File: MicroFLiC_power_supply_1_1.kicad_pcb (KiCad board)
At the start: 2 copper layers, 49.8 x 49.8 mm, 64 parts, among them P1 BARREL_JACK, P2 CONN_02X03, P3 Socket_1x14, P4 Socket_2x2, P6 JUMPER3, Q1 SI2369, Q2 TSM2314, Q3 SI2369, Q4 IRF8721, SW1 SW_PUSH_RA, U1 AP1117E33, U2 ADP2381, U3 TPS54428

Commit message: Added load resistor. Changed part references in consequence.
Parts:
- added R10: 10k, Resistors_SMD:R_0805, F.Cu at (123.2, 118.0)
- BT1: value ML2016 -> 3V LiMnO2
- C12, C13: value 10u -> 10u/10V/0.15Ω<ESR<0.5Ω
- D1, D2: value PMEG2020 -> 1N4148
- moved D1 1.27 mm to (132.6, 109.5)
- renumbered R10 to R11, R11 to R12, R12 to R13, R13 to R14, R14 to R15, R15 to R16, R16 to R17, R17 to R18
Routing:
- net /electronicSwitch/MCU_OFF: track 63.2 -> 61.9 mm
- net /electronicSwitch/PUSHBUTTON: track 25.3 -> 24.7 mm

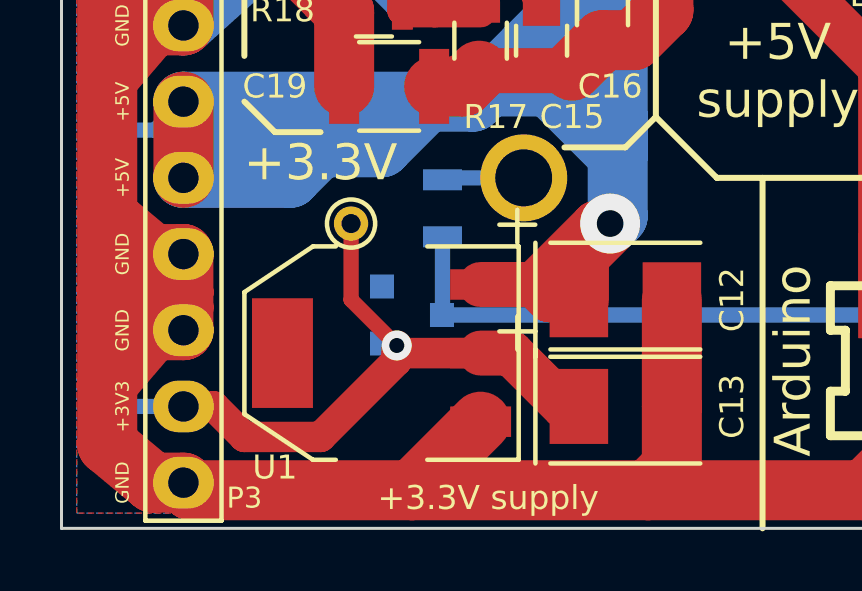
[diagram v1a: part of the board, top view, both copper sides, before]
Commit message: Changed BAR43S diode into 1N4148 for minimum leakage current.
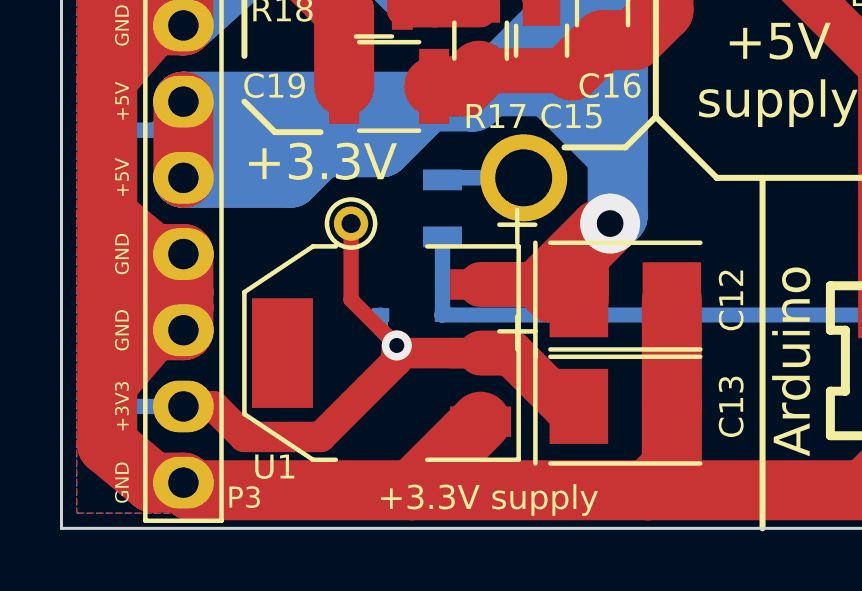
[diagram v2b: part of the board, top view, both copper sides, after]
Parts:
- D3: value BAR43S -> 1N4148; footprint Housings_SOT-23_SOT-143_TSOT-6:SOT-23 -> Diodes_SMD:SOD-323
- turned D3 to 180 degrees
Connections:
- D3 pad 1: +3V3 -> +BATT
- D3 pad 2: (no net) -> +3V3
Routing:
- net +3V3: track 23.6 -> 24.4 mm
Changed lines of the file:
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@@
   (general
     (links 140)
-    (no_connects 0)
+    (no_connects 2)
     (area 100.025999 100.025999 149.910001 149.910001)
     (thickness 1.6)
     (drawings 70)
-    (tracks 671)
+    (tracks 672)
     (zones 0)
     (modules 65)
@@
   (page A4)
   (layers
-    (0 F.Cu signal)
-    (31 B.Cu signal hide)
+    (0 F.Cu signal hide)
+    (31 B.Cu signal)
     (32 B.Adhes user)
     (33 F.Adhes user)
@@
   )
   (setup
-    (last_trace_width 0.254)
+    (last_trace_width 0.508)
     (user_trace_width 0.254)
     (user_trace_width 0.381)
@@
     )
   )
-  (module Housings_SOT-23_SOT-143_TSOT-6:SOT-23 (layer B.Cu)
-    (at 111.76 142.748 90)
-    (descr "SOT-23, Standard")
-    (tags SOT-23)
-    (attr smd)
-    (fp_text reference D3 (at 0 2.25 90) (layer B.SilkS)
-      (effects (font (size 1 1) (thickness 0.15)) (justify mirror))
-    )
-    (fp_text value BAR43S (at 0 -2.3 90) (layer B.Fab) hide
-      (effects (font (size 1 1) (thickness 0.15)) (justify mirror))
-    )
-    (fp_line (start -1.65 1.6) (end 1.65 1.6) (layer B.CrtYd) (width 0.05))
-    (fp_line (start 1.65 1.6) (end 1.65 -1.6) (layer B.CrtYd) (width 0.05))
-    (fp_line (start 1.65 -1.6) (end -1.65 -1.6) (layer B.CrtYd) (width 0.05))
-    (fp_line (start -1.65 -1.6) (end -1.65 1.6) (layer B.CrtYd) (width 0.05))
-    (fp_line (start 1.29916 0.65024) (end 1.2509 0.65024) (layer B.SilkS) (width 0.15))
-    (fp_line (start -1.49982 -0.0508) (end -1.49982 0.65024) (layer B.SilkS) (width 0.15))
-    (fp_line (start -1.49982 0.65024) (end -1.2509 0.65024) (layer B.SilkS) (width 0.15))
-    (fp_line (start 1.29916 0.65024) (end 1.49982 0.65024) (layer B.SilkS) (width 0.15))
-    (fp_line (start 1.49982 0.65024) (end 1.49982 -0.0508) (layer B.SilkS) (width 0.15))
-    (pad 1 smd rect (at -0.95 -1.00076 90) (size 0.8001 0.8001) (layers B.Cu B.Paste B.Mask)
-      (net 10 +3V3))
-    (pad 2 smd rect (at 0.95 -1.00076 90) (size 0.8001 0.8001) (layers B.Cu B.Paste B.Mask))
-    (pad 3 smd rect (at 0 0.99822 90) (size 0.8001 0.8001) (layers B.Cu B.Paste B.Mask)
-      (net 15 +BATT))
-    (model SMD_Packages.3dshapes/SOT-23_Inv.wrl
-      (at (xyz 0 0 0))
-      (scale (xyz 0.3937 0.3937 0.3937))
-      (rotate (xyz 0 0 180))
-    )
-  )
   (module jakub:ML2016 (layer B.Cu)
     (at 125.984 138.176 180)
@@
       (rotate (xyz 0 0 0))
     )
+  )
+  (module Diodes_SMD:SOD-323 (layer B.Cu)
+    (at 111.76 142.748 180)
+    (descr SOD-323)
+    (tags SOD-323)
+    (attr smd)
+    (fp_text reference D3 (at 2.286 0 180) (layer B.SilkS)
+      (effects (font (size 0.8 0.8) (thickness 0.12)) (justify mirror))
+    )
+    (fp_text value 1N4148 (at 0.1 -1.9 180) (layer B.Fab)
+      (effects (font (size 1 1) (thickness 0.15)) (justify mirror))
+    )
+    (fp_line (start 0.25 0) (end 0.5 0) (layer B.SilkS) (width 0.15))
+    (fp_line (start -0.25 0) (end -0.5 0) (layer B.SilkS) (width 0.15))
+    (fp_line (start -0.25 0) (end 0.25 0.35) (layer B.SilkS) (width 0.15))
+    (fp_line (start 0.25 0.35) (end 0.25 -0.35) (layer B.SilkS) (width 0.15))
+    (fp_line (start 0.25 -0.35) (end -0.25 0) (layer B.SilkS) (width 0.15))
+    (fp_line (start -0.25 0.35) (end -0.25 -0.35) (layer B.SilkS) (width 0.15))
+    (fp_line (start -1.5 0.95) (end 1.5 0.95) (layer B.CrtYd) (width 0.05))
+    (fp_line (start 1.5 0.95) (end 1.5 -0.95) (layer B.CrtYd) (width 0.05))
+    (fp_line (start -1.5 -0.95) (end 1.5 -0.95) (layer B.CrtYd) (width 0.05))
+    (fp_line (start -1.5 0.95) (end -1.5 -0.95) (layer B.CrtYd) (width 0.05))
+    (fp_line (start -1.3 -0.8) (end 1.1 -0.8) (layer B.SilkS) (width 0.15))
+    (fp_line (start -1.3 0.8) (end 1.1 0.8) (layer B.SilkS) (width 0.15))
+    (pad 1 smd rect (at -1.055 0 180) (size 0.59 0.45) (layers B.Cu B.Paste B.Mask)
+      (net 15 +BATT))
+    (pad 2 smd rect (at 1.055 0 180) (size 0.59 0.45) (layers B.Cu B.Paste B.Mask)
+      (net 10 +3V3))
   )
   (gr_line (start 131.572 119.888) (end 121.92 119.888) (layer F.SilkS) (width 0.2))
@@
   (segment (start 125.476 125.984) (end 127.508 128.016) (width 2) (layer F.Cu) (net 9))
   (segment (start 124.282 125.984) (end 125.476 125.984) (width 2) (layer F.Cu) (net 9))
+  (segment (start 110.705 142.748) (end 110.705 143.217) (width 0.508) (layer B.Cu) (net 10))
+  (segment (start 110.705 143.217) (end 111.252 143.764) (width 0.508) (layer B.Cu) (net 10))
   (segment (start 109.728 139.7) (end 109.728 142.24) (width 0.508) (layer F.Cu) (net 10))
   (segment (start 109.728 142.24) (end 111.252 143.764) (width 0.508) (layer F.Cu) (net 10))
@@
   (via (at 111.252 143.764) (size 1) (layers F.Cu B.Cu) (net 10))
   (segment (start 111.252 143.764) (end 111.252 144.018) (width 0.508) (layer F.Cu) (net 10))
-  (segment (start 110.75924 143.698) (end 111.186 143.698) (width 0.508) (layer B.Cu) (net 10))
   (segment (start 102.042 145.796) (end 101.6 146.238) (width 0.508) (layer B.Cu) (net 10))
   (segment (start 104.14 145.796) (end 102.042 145.796) (width 0.508) (layer B.Cu) (net 10))

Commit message: Added detailed part descriptions
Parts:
- BT1: value 3V LiMnO2 -> 3V LiMnO₂
- C1, C15, C8: value 1u -> 1u/50V
- C10, C11, C19: value 47u/6.3V -> 47u/16V
- C4: value 10u/25V -> 4u7/25V
- P1: value BARREL_JACK -> DC jack
- P2: value CONN_02X03 -> 6-way Micro-MaTch
- P3: value Socket_1x14 -> 1x14 socket strip
- P4: value Socket_2x2 -> 2x2 socket strip
- P6: value JUMPER3 -> 1x3 header strip
- SW1: value SW_PUSH_RA -> Tactile switch R/A
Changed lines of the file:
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@@
-(kicad_pcb (version 4) (host pcbnew 4.0.1-3.201512221402+6198~38~ubuntu14.04.1-stable)
+(kicad_pcb (version 4) (host pcbnew 4.0.2-4+6225~38~ubuntu14.04.1-stable)
   (general
     (links 140)
-    (no_connects 2)
+    (no_connects 0)
     (area 100.025999 100.025999 149.910001 149.910001)
     (thickness 1.6)
@@
       (effects (font (size 1 1) (thickness 0.15)) (justify mirror))
     )
-    (fp_text value "3V LiMnO2" (at 10.16 -9.652 180) (layer B.SilkS)
+    (fp_text value "3V LiMnO₂" (at 10.16 -9.652 180) (layer B.SilkS)
       (effects (font (size 1 1) (thickness 0.15)) (justify mirror))
     )
@@
       (effects (font (size 0.8 0.8) (thickness 0.12)))
     )
-    (fp_text value BARREL_JACK (at -5.08 5.588 270) (layer F.Fab) hide
+    (fp_text value "DC jack" (at -5.08 5.588 270) (layer F.Fab) hide
       (effects (font (size 1 1) (thickness 0.15)))
     )
@@
       (effects (font (size 0.8 0.8) (thickness 0.12)))
     )
-    (fp_text value CONN_02X03 (at -5.715 0 90) (layer F.SilkS) hide
+    (fp_text value "6-way Micro-MaTch" (at -5.715 0 90) (layer F.SilkS) hide
       (effects (font (size 1 1) (thickness 0.15)))
     )
@@
       (effects (font (size 0.8 0.8) (thickness 0.12)))
     )
-    (fp_text value JUMPER3 (at 0 -3.1 270) (layer F.Fab) hide
+    (fp_text value "1x3 header strip" (at 0 -3.1 270) (layer F.Fab) hide
       (effects (font (size 1 1) (thickness 0.15)))
     )
@@
       (effects (font (size 1 1) (thickness 0.15)))
     )
-    (fp_text value SW_PUSH_RA (at 0 3.175) (layer F.Fab) hide
+    (fp_text value "Tactile switch R/A" (at 0 3.175) (layer F.Fab) hide
       (effects (font (size 1 1) (thickness 0.15)))
     )
@@
       (effects (font (size 0.8 0.8) (thickness 0.12)))
     )
-    (fp_text value 1u (at 0 2.1 270) (layer F.Fab) hide
+    (fp_text value 1u/50V (at 0 2.1 270) (layer F.Fab) hide
       (effects (font (size 1 1) (thickness 0.15)))
     )
@@
       (effects (font (size 0.8 0.8) (thickness 0.12)))
     )
-    (fp_text value 47u/6.3V (at 0 2.7) (layer F.Fab) hide
+    (fp_text value 47u/16V (at 0 2.7) (layer F.Fab) hide
       (effects (font (size 1 1) (thickness 0.15)))
     )
@@
       (effects (font (size 0.7 0.7) (thickness 0.11)))
     )
-    (fp_text value 1u (at 0 2.1 180) (layer F.Fab) hide
+    (fp_text value 1u/50V (at 0 2.1 180) (layer F.Fab) hide
       (effects (font (size 1 1) (thickness 0.15)))
     )
@@
       (effects (font (size 0.8 0.8) (thickness 0.12)))
     )
-    (fp_text value 10u/25V (at 0 2.1) (layer F.Fab) hide
+    (fp_text value 4u7/25V (at 0 2.1) (layer F.Fab) hide
       (effects (font (size 1 1) (thickness 0.15)))
     )
@@
       (effects (font (size 0.8 0.8) (thickness 0.12)) (justify mirror))
     )
-    (fp_text value 1u (at 0 -2.1) (layer B.Fab) hide
+    (fp_text value 1u/50V (at 0 -2.1) (layer B.Fab) hide
       (effects (font (size 1 1) (thickness 0.15)) (justify mirror))
     )
@@
       (effects (font (size 0.8 0.8) (thickness 0.12)))
     )
-    (fp_text value 47u/6.3V (at 0 2.7 270) (layer F.Fab) hide
+    (fp_text value 47u/16V (at 0 2.7 270) (layer F.Fab) hide
       (effects (font (size 1 1) (thickness 0.15)))
     )
@@
       (effects (font (size 0.8 0.8) (thickness 0.12)))
     )
-    (fp_text value 47u/6.3V (at 0 2.7 270) (layer F.Fab) hide
+    (fp_text value 47u/16V (at 0 2.7 270) (layer F.Fab) hide
       (effects (font (size 1 1) (thickness 0.15)))
     )
@@
       (effects (font (size 0.7 0.7) (thickness 0.11)))
     )
-    (fp_text value Socket_1x14 (at 0 -3.1) (layer F.Fab) hide
+    (fp_text value "1x14 socket strip" (at 0 -3.1) (layer F.Fab) hide
       (effects (font (size 1 1) (thickness 0.15)))
     )
@@
       (effects (font (size 0.7 0.7) (thickness 0.11)) (justify mirror))
     )
-    (fp_text value Socket_2x2 (at 0 3.1) (layer B.Fab) hide
+    (fp_text value "2x2 socket strip" (at 0 3.1) (layer B.Fab) hide
       (effects (font (size 1 1) (thickness 0.15)) (justify mirror))
     )
